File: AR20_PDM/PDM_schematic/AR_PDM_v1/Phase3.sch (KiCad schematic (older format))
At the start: 10 parts, among them Q2 BTS50025-1TAD, U3 INA233

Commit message: Working on pcb layout
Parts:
- removed D?: D_Schottky_x2, symbol AR20_PDM_v1-rescue:D_Schottky_x2
- added D43, D44: D_Schottky_BAT60A, AR_PDM_v1:D_Shotky_BAT60_HandSoldering, symbol AR20_PDM_v1-rescue:D_Schottky_BAT60A
- gave numbers to parts that had none: 4
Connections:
- net GND: now also D43.2 (A), D44.2 (A)
- net at R20.1, U3.10 (IN+): now also D44.1 (K)
- net at R16.1, U3.9 (In-): now also D43.1 (K)
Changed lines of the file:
@@
 AR Path="/5E0E607C/5EE8C171" Ref="R?"  Part="1"
 AR Path="/5E0FB5C8/5EE8C171" Ref="R?"  Part="1"
-AR Path="/5E0FBBBD/5EE8C171" Ref="R?"  Part="1"
+AR Path="/5E0FBBBD/5EE8C171" Ref="R17"  Part="1"
 AR Path="/5E0FC3A2/5EE8C171" Ref="R?"  Part="1"
 AR Path="/5E0FCFDC/5EE8C171" Ref="R?"  Part="1"
 AR Path="/5E0FDCCC/5EE8C171" Ref="R?"  Part="1"
 AR Path="/5E10174B/5EE8C171" Ref="R?"  Part="1"
-F 0 "R?" V 6643 1600 50  0000 C CNN
+F 0 "R17" V 6643 1600 50  0000 C CNN
 F 1 "2m_1%_4W" V 6734 1600 50  0000 C CNN
 F 2 "Resistor_SMD:R_2512_6332Metric" V 6780 1600 50  0001 C CNN
@@
 Text HLabel 7300 1600 2    50   Input ~ 10
 V+12V
-$Comp
-L AR20_PDM_v1-rescue:D_Schottky_x2 D?
-U 1 1 5EE8C178
-P 6950 4825
-AR Path="/5DA89415/5EE8C178" Ref="D?"  Part="1"
-AR Path="/5E0FBBBD/5EE8C178" Ref="D?"  Part="1"
-F 0 "D?" H 6950 5041 50  0000 C CNN
-F 1 "D_Schottky_x2" H 6950 4950 50  0000 C CNN
-F 2 "" H 6950 4825 50  0001 C CNN
-F 3 "~" H 6950 4825 50  0001 C CNN
-	1    6950 4825
-	1    0    0    -1
-$EndComp
 $Comp
 L AR20_PDM_v1-rescue:R-Device R?
@@
 AR Path="/5E0E607C/5EE8C17E" Ref="R?"  Part="1"
 AR Path="/5E0FB5C8/5EE8C17E" Ref="R?"  Part="1"
-AR Path="/5E0FBBBD/5EE8C17E" Ref="R?"  Part="1"
+AR Path="/5E0FBBBD/5EE8C17E" Ref="R16"  Part="1"
 AR Path="/5E0FC3A2/5EE8C17E" Ref="R?"  Part="1"
 AR Path="/5E0FCFDC/5EE8C17E" Ref="R?"  Part="1"
 AR Path="/5E0FDCCC/5EE8C17E" Ref="R?"  Part="1"
 AR Path="/5E10174B/5EE8C17E" Ref="R?"  Part="1"
-F 0 "R?" V 6443 3850 50  0000 C CNN
+F 0 "R16" V 6443 3850 50  0000 C CNN
 F 1 "1K_1%" V 6534 3850 50  0000 C CNN
 F 2 "Resistor_SMD:R_0603_1608Metric" V 6580 3850 50  0001 C CNN
@@
 AR Path="/5E0E607C/5EE8C184" Ref="R?"  Part="1"
 AR Path="/5E0FB5C8/5EE8C184" Ref="R?"  Part="1"
-AR Path="/5E0FBBBD/5EE8C184" Ref="R?"  Part="1"
+AR Path="/5E0FBBBD/5EE8C184" Ref="R20"  Part="1"
 AR Path="/5E0FC3A2/5EE8C184" Ref="R?"  Part="1"
 AR Path="/5E0FCFDC/5EE8C184" Ref="R?"  Part="1"
 AR Path="/5E0FDCCC/5EE8C184" Ref="R?"  Part="1"
 AR Path="/5E10174B/5EE8C184" Ref="R?"  Part="1"
-F 0 "R?" V 6843 3850 50  0000 C CNN
+F 0 "R20" V 6843 3850 50  0000 C CNN
 F 1 "1K_1%" V 6934 3850 50  0000 C CNN
 F 2 "Resistor_SMD:R_0603_1608Metric" V 6980 3850 50  0001 C CNN
@@
 Text Notes 7075 2000 0    50   ~ 10
 Place shunt and INA233 close, \nroute togethere, differentialy pair. \nKeep short, and away from Noise.
-$Comp
-L AR20_PDM_v1-rescue:GND-power #PWR?
-U 1 1 5EE8C192
-P 6950 5025
-AR Path="/5DA89415/5EE8C192" Ref="#PWR?"  Part="1"
-AR Path="/5DEB10A1/5EE8C192" Ref="#PWR?"  Part="1"
-AR Path="/5DEB20EA/5EE8C192" Ref="#PWR?"  Part="1"
-AR Path="/5E0E4725/5EE8C192" Ref="#PWR?"  Part="1"
-AR Path="/5E0E4A93/5EE8C192" Ref="#PWR?"  Part="1"
-AR Path="/5E0E4EB5/5EE8C192" Ref="#PWR?"  Part="1"
-AR Path="/5E0E5304/5EE8C192" Ref="#PWR?"  Part="1"
-AR Path="/5E0E594B/5EE8C192" Ref="#PWR?"  Part="1"
-AR Path="/5E0E607C/5EE8C192" Ref="#PWR?"  Part="1"
-AR Path="/5E0FB5C8/5EE8C192" Ref="#PWR?"  Part="1"
-AR Path="/5E0FBBBD/5EE8C192" Ref="#PWR?"  Part="1"
-AR Path="/5E0FC3A2/5EE8C192" Ref="#PWR?"  Part="1"
-AR Path="/5E0FCFDC/5EE8C192" Ref="#PWR?"  Part="1"
-AR Path="/5E0FDCCC/5EE8C192" Ref="#PWR?"  Part="1"
-AR Path="/5E10174B/5EE8C192" Ref="#PWR?"  Part="1"
-F 0 "#PWR?" H 6950 4775 50  0001 C CNN
-F 1 "GND" H 6955 4852 50  0000 C CNN
-F 2 "" H 6950 5025 50  0001 C CNN
-F 3 "" H 6950 5025 50  0001 C CNN
-	1    6950 5025
-	1    0    0    -1
-$EndComp
 Wire Wire Line
 	4775 1600 6650 1600
@@
 Wire Wire Line
 	6650 4400 8750 4400
-Connection ~ 6650 4400
-Wire Wire Line
-	6650 4400 6650 4825
-Wire Wire Line
-	8750 4300 7250 4300
-Wire Wire Line
-	7250 4825 7250 4300
-Connection ~ 7250 4300
-Wire Wire Line
-	7250 4300 7050 4300
 $Comp
 L AR20_PDM_v1-rescue:R-Device R?
@@
 AR Path="/5E0E607C/5EEC2C35" Ref="R?"  Part="1"
 AR Path="/5E0FB5C8/5EEC2C35" Ref="R?"  Part="1"
-AR Path="/5E0FBBBD/5EEC2C35" Ref="R?"  Part="1"
+AR Path="/5E0FBBBD/5EEC2C35" Ref="R21"  Part="1"
 AR Path="/5E0FC3A2/5EEC2C35" Ref="R?"  Part="1"
 AR Path="/5E0FCFDC/5EEC2C35" Ref="R?"  Part="1"
 AR Path="/5E0FDCCC/5EEC2C35" Ref="R?"  Part="1"
 AR Path="/5E10174B/5EEC2C35" Ref="R?"  Part="1"
-F 0 "R?" V 8093 4100 50  0000 C CNN
+F 0 "R21" V 8093 4100 50  0000 C CNN
 F 1 "10K" V 8184 4100 50  0000 C CNN
 F 2 "Resistor_SMD:R_0603_1608Metric" V 8230 4100 50  0001 C CNN
@@
 Text HLabel 8150 4100 0    50   Output ~ 10
 P3_OUT
+Wire Wire Line
+	7050 4300 7100 4300
+$Comp
+L AR20_PDM_v1-rescue:D_Schottky_BAT60A D?
+U 1 1 5EFA5345
+P 6700 4775
+AR Path="/5DA89415/5EFA5345" Ref="D?"  Part="1"
+AR Path="/5E0FBBBD/5EFA5345" Ref="D43"  Part="1"
+F 0 "D43" V 6530 4885 50  0000 L CNN
+F 1 "D_Schottky_BAT60A" V 6621 4885 50  0000 L CNN
+F 2 "AR_PDM_v1:D_Shotky_BAT60_HandSoldering" H 6800 4725 50  0001 C CNN
+F 3 "~" H 6800 4725 50  0001 C CNN
+	1    6700 4775
+	0    1    1    0
+$EndComp
+$Comp
+L AR20_PDM_v1-rescue:GND-power #PWR?
+U 1 1 5EFA534B
+P 6875 4950
+AR Path="/5DA89415/5EFA534B" Ref="#PWR?"  Part="1"
+AR Path="/5DEB10A1/5EFA534B" Ref="#PWR?"  Part="1"
+AR Path="/5DEB20EA/5EFA534B" Ref="#PWR?"  Part="1"
+AR Path="/5E0E4725/5EFA534B" Ref="#PWR?"  Part="1"
+AR Path="/5E0E4A93/5EFA534B" Ref="#PWR?"  Part="1"
+AR Path="/5E0E4EB5/5EFA534B" Ref="#PWR?"  Part="1"
+AR Path="/5E0E5304/5EFA534B" Ref="#PWR?"  Part="1"
+AR Path="/5E0E594B/5EFA534B" Ref="#PWR?"  Part="1"
+AR Path="/5E0E607C/5EFA534B" Ref="#PWR?"  Part="1"
+AR Path="/5E0FB5C8/5EFA534B" Ref="#PWR?"  Part="1"
+AR Path="/5E0FBBBD/5EFA534B" Ref="#PWR04"  Part="1"
+AR Path="/5E0FC3A2/5EFA534B" Ref="#PWR?"  Part="1"
+AR Path="/5E0FCFDC/5EFA534B" Ref="#PWR?"  Part="1"
+AR Path="/5E0FDCCC/5EFA534B" Ref="#PWR?"  Part="1"
+AR Path="/5E10174B/5EFA534B" Ref="#PWR?"  Part="1"
+F 0 "#PWR04" H 6875 4700 50  0001 C CNN
+F 1 "GND" H 6880 4777 50  0000 C CNN
+F 2 "" H 6875 4950 50  0001 C CNN
+F 3 "" H 6875 4950 50  0001 C CNN
+	1    6875 4950
+	1    0    0    -1
+$EndComp
+$Comp
+L AR20_PDM_v1-rescue:D_Schottky_BAT60A D?
+U 1 1 5EFA5351
+P 7150 4775
+AR Path="/5DA89415/5EFA5351" Ref="D?"  Part="1"
+AR Path="/5E0FBBBD/5EFA5351" Ref="D44"  Part="1"
+F 0 "D44" V 6980 4885 50  0000 L CNN
+F 1 "D_Schottky_BAT60A" V 7071 4885 50  0000 L CNN
+F 2 "AR_PDM_v1:D_Shotky_BAT60_HandSoldering" H 7250 4725 50  0001 C CNN
+F 3 "~" H 7250 4725 50  0001 C CNN
+	1    7150 4775
+	0    1    1    0
+$EndComp
+Wire Wire Line
+	6650 4475 6650 4400
+Wire Wire Line
+	7100 4475 7100 4300
+Wire Wire Line
+	6650 4825 6875 4825
+Wire Wire Line
+	6875 4950 6875 4825
+Connection ~ 6875 4825
+Wire Wire Line
+	6875 4825 7100 4825
+Connection ~ 7100 4300
+Wire Wire Line
+	7100 4300 8750 4300
+Connection ~ 6650 4400
 $EndSCHEMATC

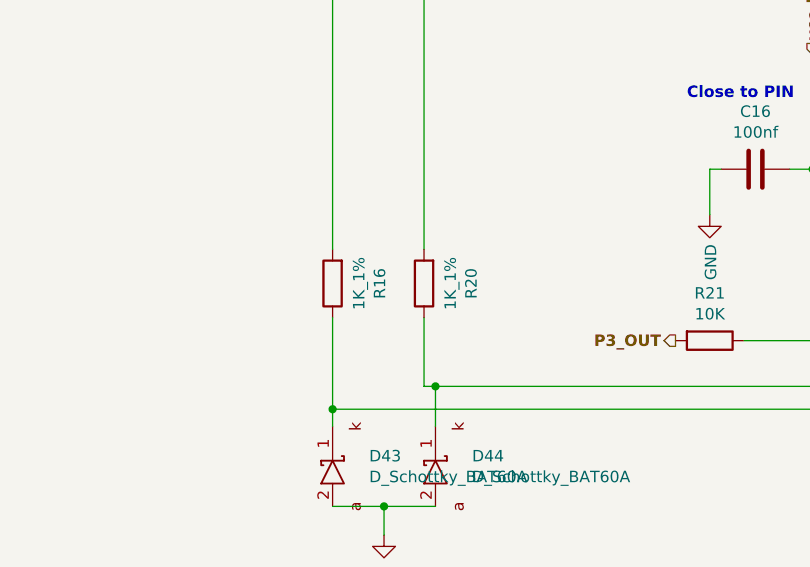
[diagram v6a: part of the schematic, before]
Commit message: shematics adjustments, and fixing values and names
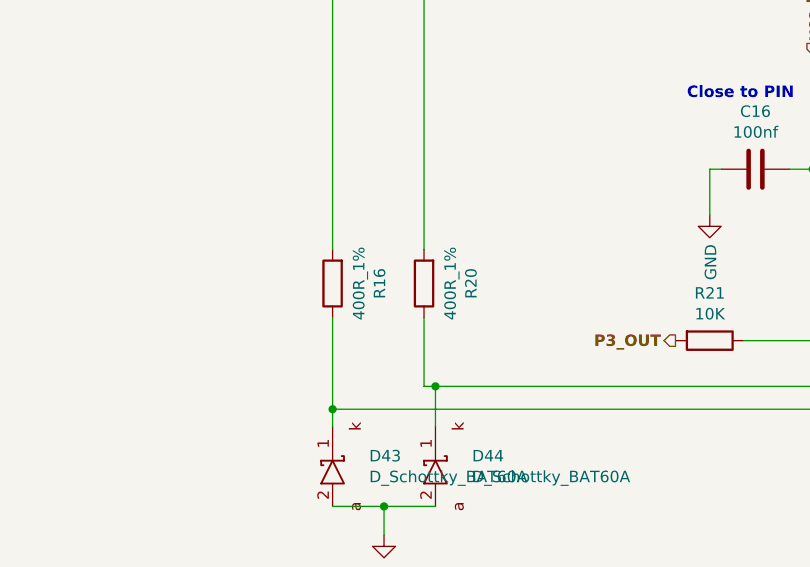
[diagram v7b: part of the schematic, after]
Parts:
- R16, R20: value 1K_1% -> 400R_1%
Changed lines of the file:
@@
 AR Path="/5E10174B/5EE8C17E" Ref="R?"  Part="1"
 F 0 "R16" V 6443 3850 50  0000 C CNN
-F 1 "1K_1%" V 6534 3850 50  0000 C CNN
+F 1 "400R_1%" V 6534 3850 50  0000 C CNN
 F 2 "Resistor_SMD:R_0603_1608Metric" V 6580 3850 50  0001 C CNN
 F 3 "~" H 6650 3850 50  0001 C CNN
@@
 AR Path="/5E10174B/5EE8C184" Ref="R?"  Part="1"
 F 0 "R20" V 6843 3850 50  0000 C CNN
-F 1 "1K_1%" V 6934 3850 50  0000 C CNN
+F 1 "400R_1%" V 6934 3850 50  0000 C CNN
 F 2 "Resistor_SMD:R_0603_1608Metric" V 6980 3850 50  0001 C CNN
 F 3 "~" H 7050 3850 50  0001 C CNN
